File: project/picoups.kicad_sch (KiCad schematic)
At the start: 26 parts, among them J1 Conn_02x20_Odd_Even, J2 BATT, J3 VIN, J4 VOUT, U1 LT3652EMSE

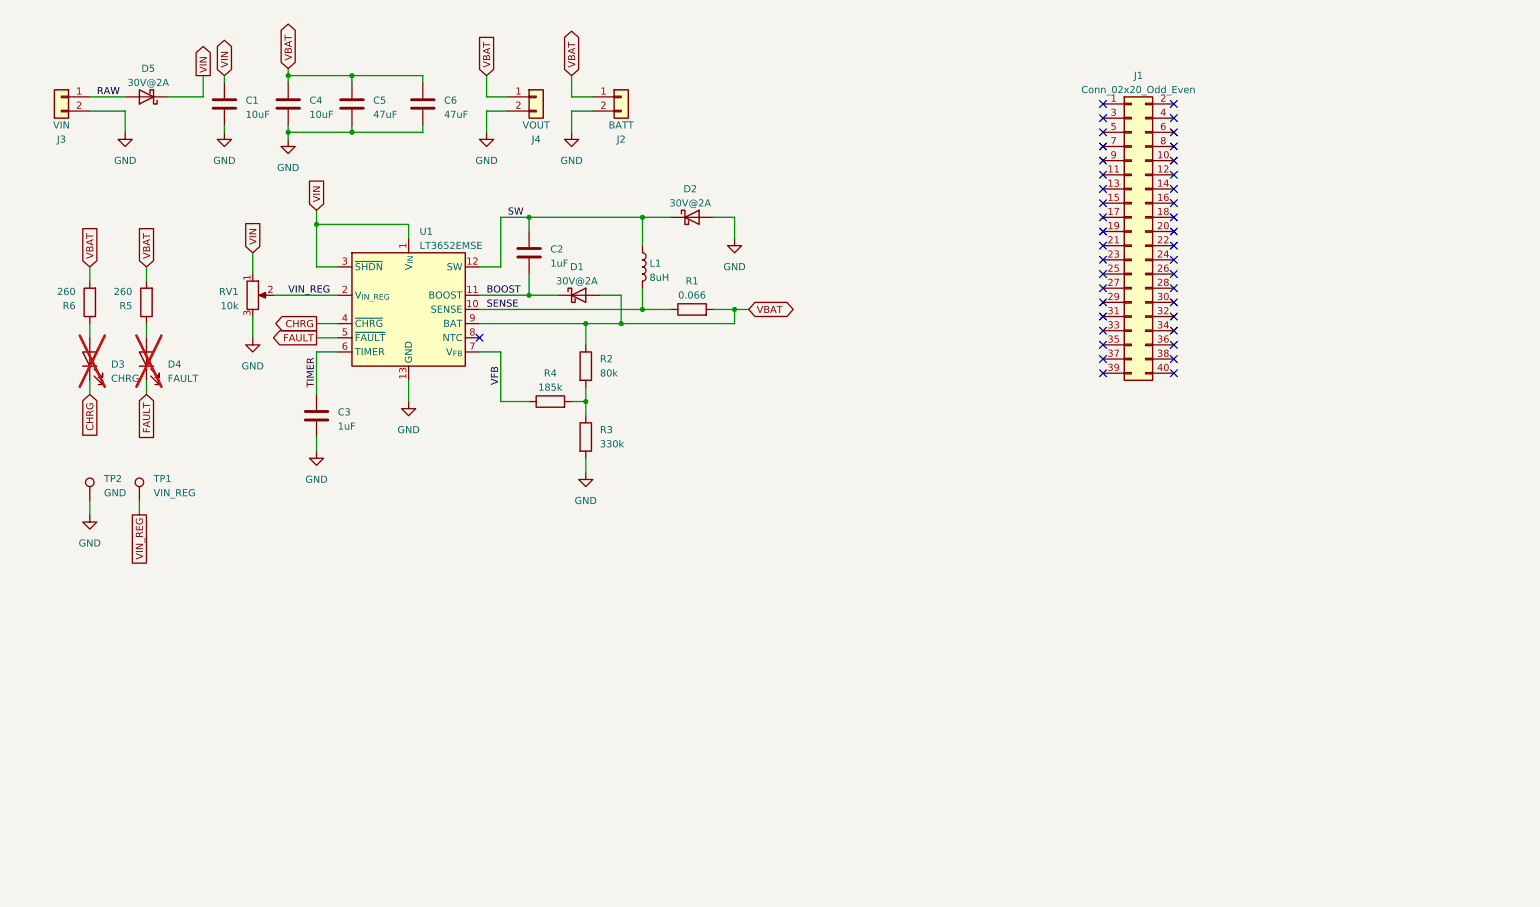
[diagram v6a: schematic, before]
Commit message: Added boost converter and power monitor
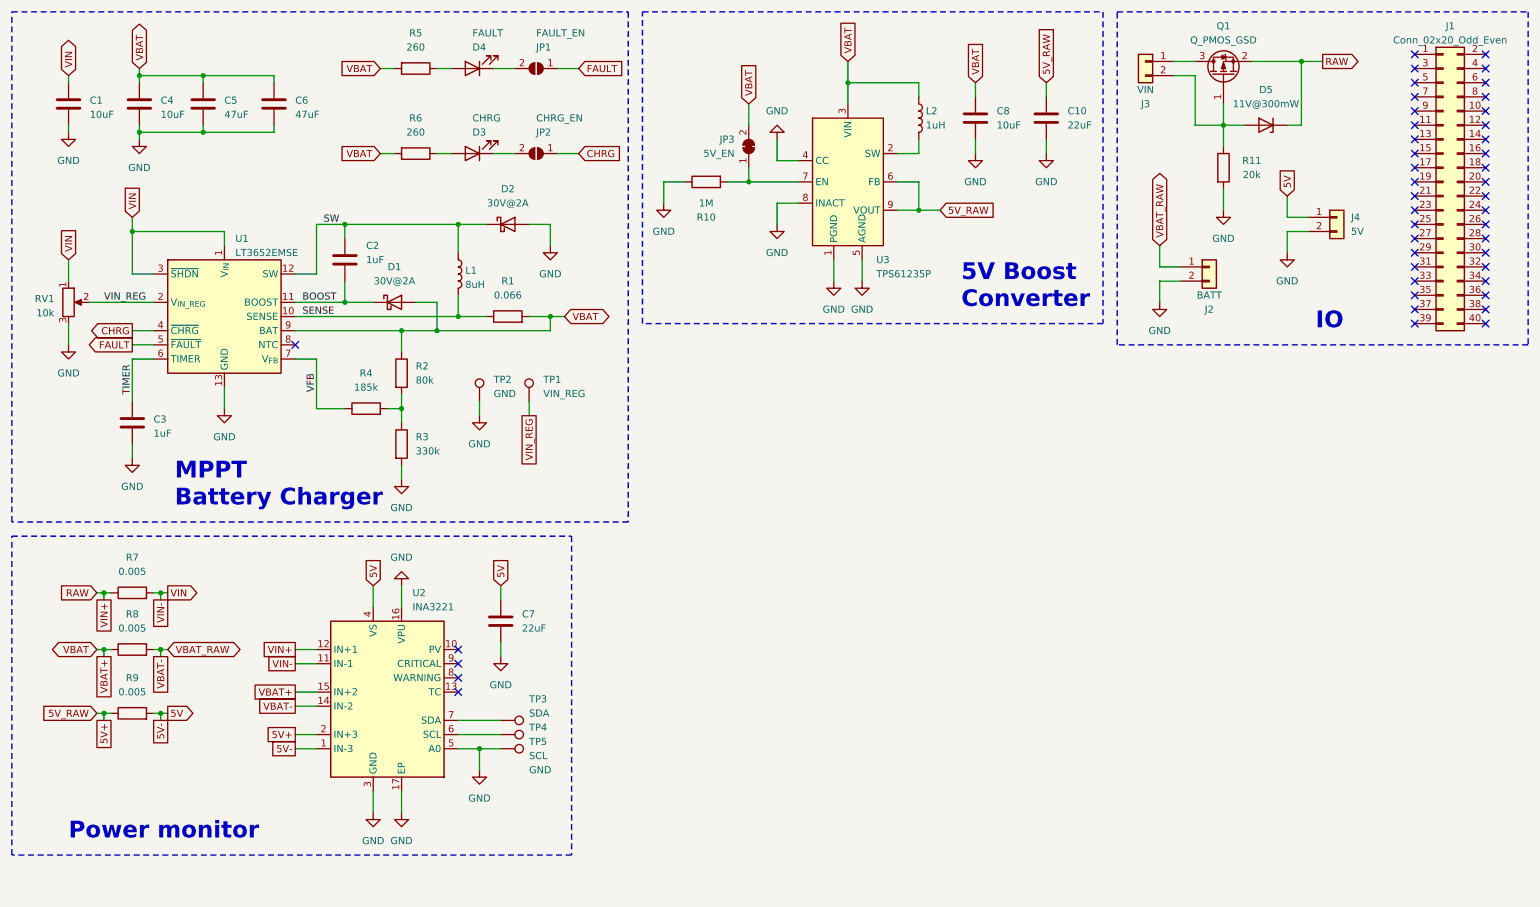
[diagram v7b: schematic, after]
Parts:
- removed D5: 30V@2A, Diode_SMD:D_MicroSMP_AK, symbol Device:D_Schottky
- added C10, C7: 22uF, Capacitor_SMD:C_0805_2012Metric, symbol Device:C
- added C8: 10uF, Capacitor_SMD:C_0805_2012Metric, symbol Device:C
- added D5: 11V@300mW, Diode_SMD:D_SOD-323, symbol Device:D_Zener
- added JP1: FAULT_EN, Jumper:SolderJumper-2_P1.3mm_Open_RoundedPad1.0x1.5mm, symbol Jumper:SolderJumper_2_Open
- added JP2: CHRG_EN, Jumper:SolderJumper-2_P1.3mm_Open_RoundedPad1.0x1.5mm, symbol Jumper:SolderJumper_2_Open
- added JP3: 5V_EN, Jumper:SolderJumper-2_P1.3mm_Bridged_RoundedPad1.0x1.5mm, symbol Jumper:SolderJumper_2_Bridged
- added L2: 1uH, Inductor_SMD:L_Vishay_IHLP-2020, symbol Device:L
- added Q1: Q_PMOS_GSD, Package_TO_SOT_SMD:SOT-23, symbol Device:Q_PMOS_GSD
- added R10: 1M, Resistor_SMD:R_0805_2012Metric, symbol Device:R
- added R11: 20k, Resistor_SMD:R_0805_2012Metric, symbol Device:R
- added R7, R8, R9: 0.005, Resistor_SMD:R_1210_3225Metric, symbol Device:R
- added TP3: SDA, TestPoint:TestPoint_Pad_D2.0mm, symbol Connector:TestPoint
- added TP4: SCL, TestPoint:TestPoint_Pad_D2.0mm, symbol Connector:TestPoint
- added TP5: GND, TestPoint:TestPoint_Pad_D2.0mm, symbol Connector:TestPoint
- added U2: INA3221, Package_DFN_QFN:Texas_RGV_S-PVQFN-N16_EP2.1x2.1mm, symbol Power_Management:INA3221
- added U3: TPS61235P, PicoUPS:TPS61235P, symbol PicoUPS:TPS61235P
- D3, D4: now fitted
- J4: value VOUT -> 5V
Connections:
- net CHRG: now also JP2.1 (A); no longer D3.1 (K)
- net FAULT: now also JP1.1 (A); no longer D4.1 (K)
- net GND: now also C10.2, C7.2, C8.2, R10.1, R11.2, TP5.1, U2.16 (VPU), U2.17 (EP), U2.3 (GND), U2.5 (A0), U3.1 (PGND), U3.4 (CC), U3.5 (AGND), U3.8 (INACT); no longer J3.2 (Pin_2)
- net RAW: now also D5.1 (K), Q1.2 (S), R7.1, U2.12 (IN+1); no longer J3.1 (Pin_1)
- net VBAT: now also C8.1, JP3.2 (B), L2.1, R8.1, U2.15 (IN+2), U3.3 (VIN); no longer J2.1 (Pin_1), J4.1 (Pin_1)
- net VIN: now also R7.2, U2.11 (IN-1)
- new net: JP3.1 (A), R10.2, U3.7 (EN)
- new net: TP4.1, U2.6 (SCL)
- new net: TP3.1, U2.7 (SDA)
- new net: D3.1 (K), JP2.2 (B)
- new net: D4.1 (K), JP1.2 (B)
- new net: L2.2, U3.2 (SW)
- new net: D5.2 (A), J3.2 (Pin_2), Q1.1 (G), R11.1
- new net: J3.1 (Pin_1), Q1.3 (D)
- new net 5V: C7.1, J4.1 (Pin_1), R9.2, U2.1 (IN-3), U2.4 (VS)
- new net 5V+: C10.1, R9.1, U2.2 (IN+3), U3.6 (FB), U3.9 (VOUT)
- new net VBAT-: J2.1 (Pin_1), R8.2, U2.14 (IN-2)
- no-connect marks 41 -> 45
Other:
- note added: "5V Boost Converter"
- note added: "IO"
- note added: "MPPT Battery Charger"
- note added: "Power monitor"
- moved on the sheet: C1, C2, C3, C4, C5, C6, D1, D2, J1, J2, J3, J4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

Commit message: Added components
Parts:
- removed JP3: 5V_EN, Jumper:SolderJumper-2_P1.3mm_Bridged_RoundedPad1.0x1.5mm, symbol Jumper:SolderJumper_2_Bridged
- removed R10: 1M, Resistor_SMD:R_0805_2012Metric, symbol Device:R
- D1, D2: value 30V@2A -> 30V@3A; footprint Diode_SMD:D_MicroSMP_AK -> Diode_SMD:D_SOD-123F
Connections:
- net 5V: now also U2.11 (IN-1); no longer U2.1 (IN-3)
- net 5V+: now also U2.12 (IN+1); no longer U2.2 (IN+3)
- net GND: now also J3.2 (Pin_2)
- net RAW: now also U2.2 (IN+3); no longer U2.12 (IN+1)
- net VBAT: now also U3.7 (EN)
- net VIN: now also U2.1 (IN-3); no longer U2.11 (IN-1)
- net at D5.2 (A), Q1.1 (G), R11.1: no longer J3.2 (Pin_2)
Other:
- moved on the sheet: C10, C8, L2, U3
